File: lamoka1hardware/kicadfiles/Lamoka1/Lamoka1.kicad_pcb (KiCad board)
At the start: 2 copper layers, 26 parts

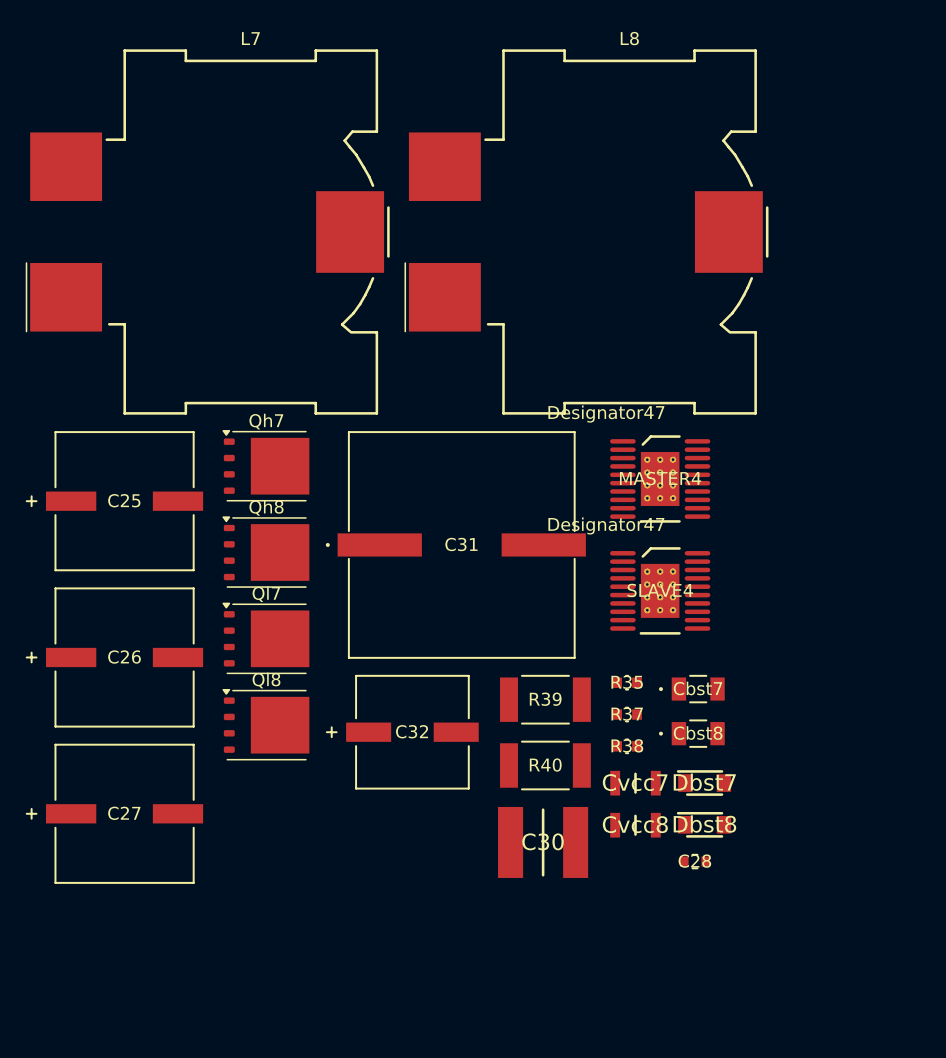
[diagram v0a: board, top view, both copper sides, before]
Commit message: ADD the schematic for testing the boost section is all done and configured
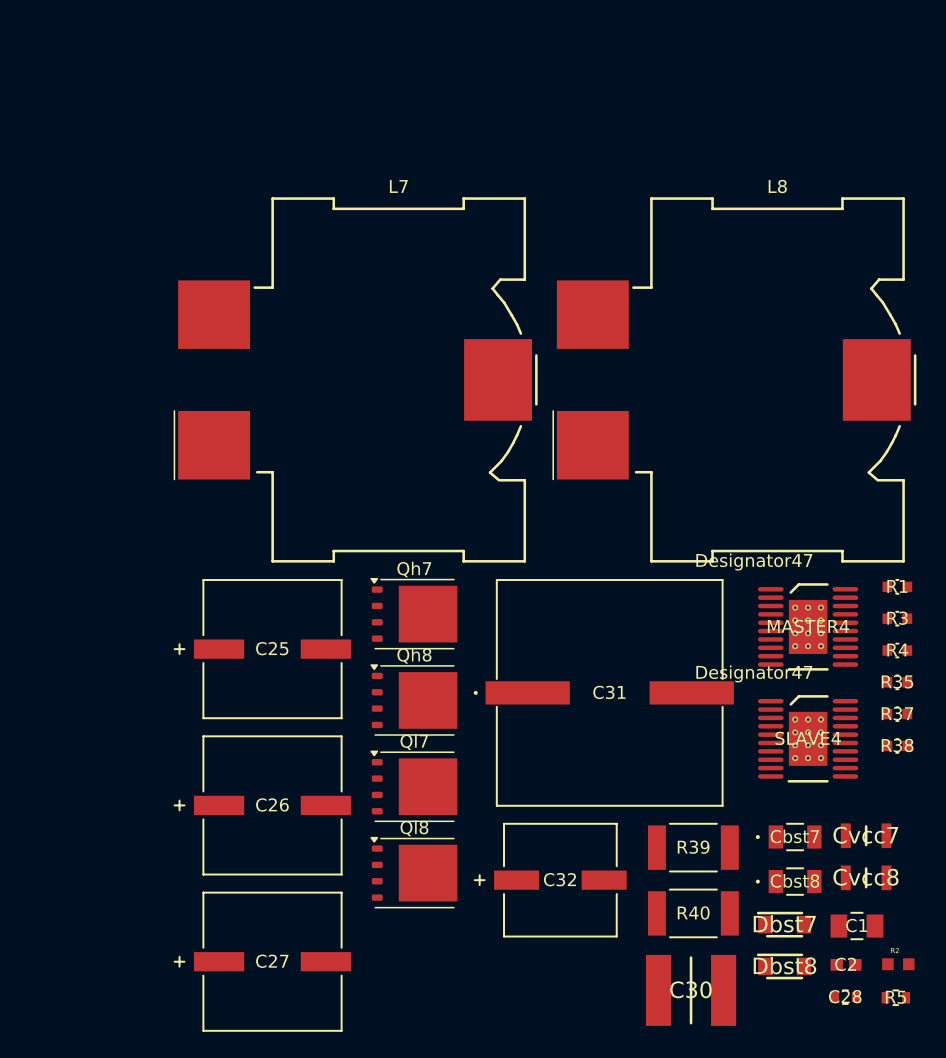
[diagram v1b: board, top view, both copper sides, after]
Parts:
- added C1: C1206C474K5RACTU, Components:CAPC340180_100N_KEM, F.Cu at (176.1, 130.3)
- added C2: CC0603KRX7R9BB223, Components:YAG_CC0603_YAG, F.Cu at (175.3, 133.3)
- added R1: RC0603FR-0756K2L, Components:RC0603N_YAG, F.Cu at (179.3, 103.9)
- added R2: RN73R1JTTD1842F25, Components:RESC1608X55N, F.Cu at (179.3, 133.3)
- added R3: RC0603FR-07392KL, Components:RC0603N_YAG, F.Cu at (179.3, 106.4)
- added R4: RC0603FR-0710KL, Components:RC0603N_YAG, F.Cu at (179.3, 108.9)
- added R5: RN73R1JTTD4992F25, Components:RES_RN73R_1J_KOA, F.Cu at (179.1, 135.9)
- moved R35 21.0 mm to (179.3, 111.4)
- moved R37 21.0 mm to (179.3, 113.8)
- moved R38 21.0 mm to (179.3, 116.3)
- moved Cvcc7 18.4 mm to (176.8, 123.3)
- moved Cvcc8 18.4 mm to (176.8, 126.6)
- moved C27 16.3 mm to (130.7, 133.1)
- moved C25 16.3 mm to (130.7, 108.8)
- moved C26 16.3 mm to (130.7, 120.9)
- moved R40 16.3 mm to (163.4, 129.3)
- moved C30 16.3 mm to (163.2, 135.3)
- moved C31 16.3 mm to (156.9, 112.2)
- moved C32 16.3 mm to (153.1, 126.7)
- moved L7 16.3 mm to (140.5, 87.8)
- moved L8 16.3 mm to (169.9, 87.8)
- moved MASTER4 16.3 mm to (172.3, 107.0)
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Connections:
- net /Boost/VIN-SOURCE renamed /BOOST-SECTION/VIN-SOURCE
- net Net-(Qh7-D) renamed /BOOST-SECTION/VOUT-BOOST
